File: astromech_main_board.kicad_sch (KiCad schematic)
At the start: 15 parts, among them IC2 MAX11645EUA+, J1 Screw_Terminal_01x02, J2 Screw_Terminal_01x02, J3 Screw_Terminal_01x02, U8 NCP1117-3.3_SOT223, U9 NCP1117-5.0_TO252

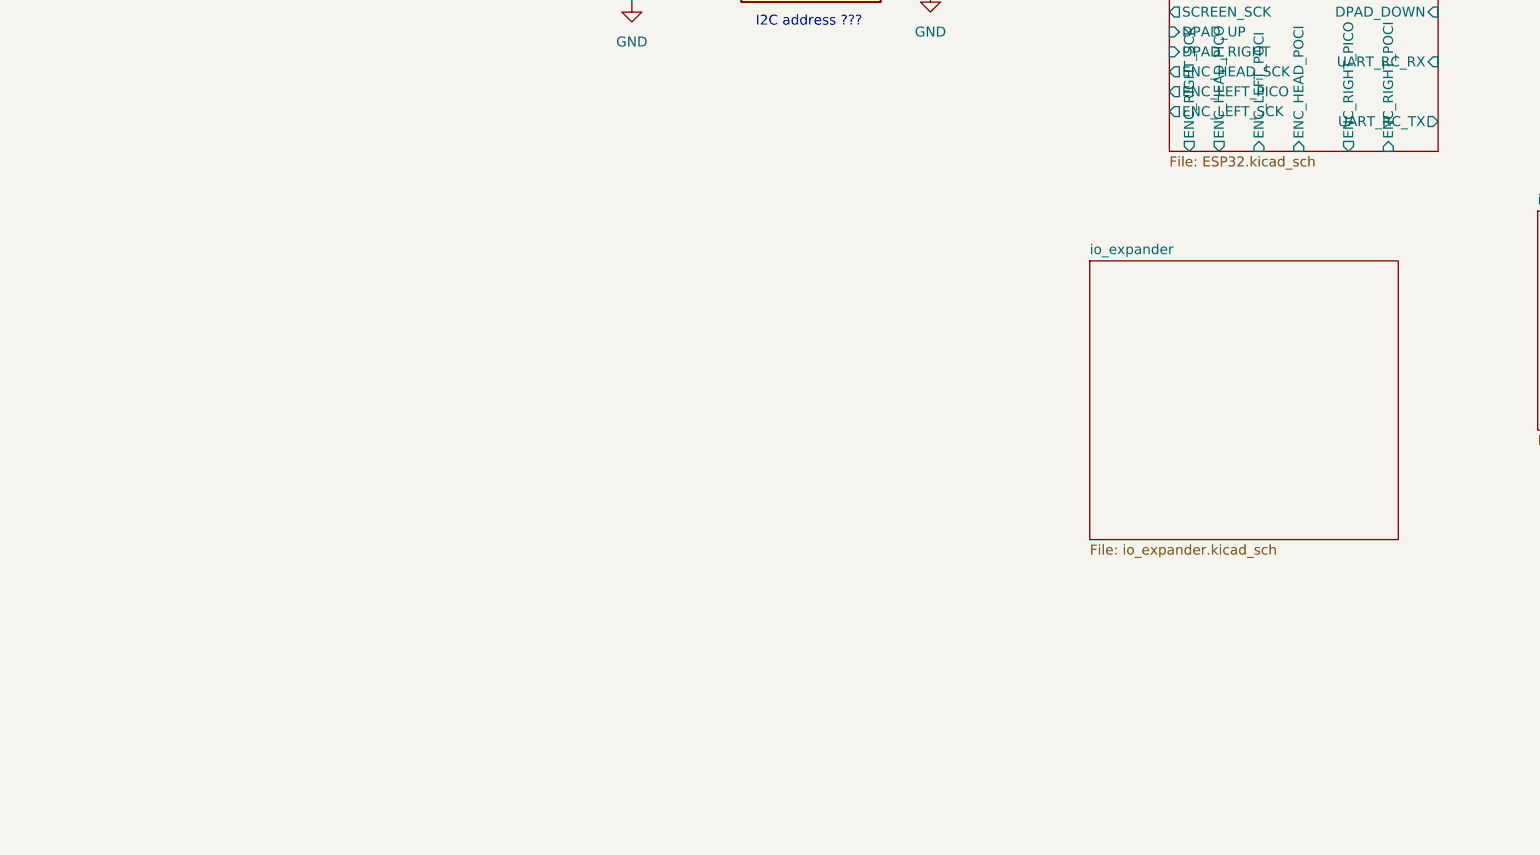
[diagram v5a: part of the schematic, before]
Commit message: moved io expander
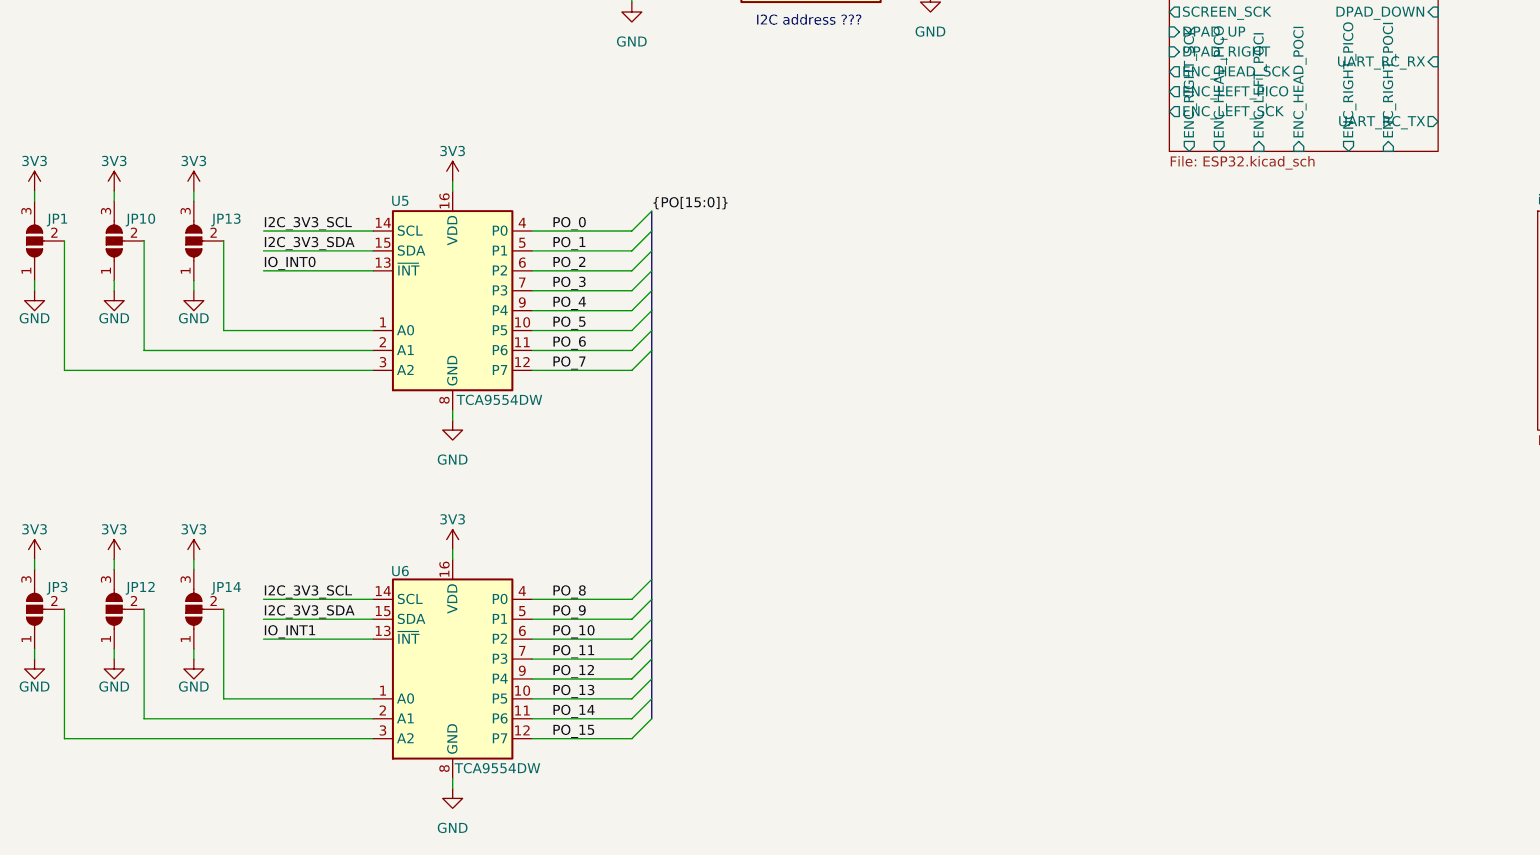
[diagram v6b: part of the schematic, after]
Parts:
- added JP1, JP10, JP12, JP13, JP14, JP3: SolderJumper_3_Open, symbol Jumper:SolderJumper_3_Open
- added U5, U6: TCA9554DW, Package_SO:SOIC-16W_7.5x10.3mm_P1.27mm, symbol Interface_Expansion:TCA9554DW
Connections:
- net 3V3: now also JP1.3 (B), JP10.3 (B), JP12.3 (B), JP13.3 (B), JP14.3 (B), JP3.3 (B), U5.16 (VDD), U6.16 (VDD)
- net GND: now also JP1.1 (A), JP10.1 (A), JP12.1 (A), JP13.1 (A), JP14.1 (A), JP3.1 (A), U5.8 (GND), U6.8 (GND)
- new net: JP1.2 (C), U5.3 (A2)
- new net: JP13.2 (C), U5.1 (A0)
- new net: JP14.2 (C), U6.1 (A0)
- new net: JP12.2 (C), U6.2 (A1)
- new net: JP3.2 (C), U6.3 (A2)
- new net: JP10.2 (C), U5.2 (A1)
- new net I2C_3V3_SCL: U5.14 (SCL), U6.14 (SCL)
- new net I2C_3V3_SDA: U5.15 (SDA), U6.15 (SDA)
- new net IO_INT0: U5.13 (~{INT})
- new net IO_INT1: U6.13 (~{INT})
- new net PO_0: U5.4 (P0)
- new net PO_1: U5.5 (P1)
- new net PO_10: U6.6 (P2)
- new net PO_11: U6.7 (P3)
- new net PO_12: U6.9 (P4)
- new net PO_13: U6.10 (P5)
- new net PO_14: U6.11 (P6)
- new net PO_15: U6.12 (P7)
- new net PO_2: U5.6 (P2)
- new net PO_3: U5.7 (P3)
- new net PO_4: U5.9 (P4)
- new net PO_5: U5.10 (P5)
- new net PO_6: U5.11 (P6)
- new net PO_7: U5.12 (P7)
- new net PO_8: U6.4 (P0)
- new net PO_9: U6.5 (P1)
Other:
- removed sheet io_expander

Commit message: moved encoder
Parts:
- added C2, C4: C_Small, symbol Device:C_Small
- added JP2, JP4, JP5, JP6: SolderJumper_2_Bridged, symbol Jumper:SolderJumper_2_Bridged
- added R6: R_Small_US, symbol Device:R_Small_US
- added R7: 1M, symbol Device:R_US
- added U10, U11, U7: LS7366R, LS7366R:DIP762W45P254L1917H533Q14, symbol LS7366R:LS7366R
- added U12: 74HC14, symbol 74xx:74HC14
- added Y1: Crystal, symbol Device:Crystal
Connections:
- net I2C_5V_SCL is gone; now on net I2C_3V3_SCL: IC2.5 (SCL)
- net I2C_5V_SDA is gone; now on net I2C_3V3_SDA: IC2.6 (SDA)
- net 3V3: now also IC2.8 (VDD), R6.1
- net 5V: now also U10.14 (VDD), U11.14 (VDD), U12.14 (VCC), U7.14 (VDD); no longer IC2.8 (VDD)
- net GND: now also C2.1, C4.1, U10.3 (VSS), U11.3 (VSS), U12.7 (GND), U7.3 (VSS)
- new net: JP5.1 (A), JP6.1 (A), U12.2
- new net: JP6.2 (B), U7.2 (FCKI)
- new net: C2.2, JP4.1 (A), R7.1, Y1.2
- new net: JP4.2 (B), U11.2 (FCKI)
- new net: C4.2, JP2.1 (A), R7.2, U12.1, Y1.1
- new net: JP5.2 (B), U10.2 (FCKI)
- new net: JP2.2 (B), U11.1 (FCKO)
- new net ENC_CNT_EN: U10.13 (CNT_EN), U11.13 (CNT_EN), U7.13 (CNT_EN)
- new net ENC_INT: R6.2, U10.8 (LFLAG/), U11.8 (LFLAG/), U7.8 (LFLAG/)
- new net HEAD_A: U11.12 (A)
- new net HEAD_B: U11.11 (B)
- new net HEAD_INDEX: U11.10 (INDEX/)
- new net LEFT_A: U10.12 (A)
- new net LEFT_B: U10.11 (B)
- new net LEFT_INDEX: U10.10 (INDEX/)
- new net RIGHT_A: U7.12 (A)
- new net RIGHT_B: U7.11 (B)
- new net RIGHT_INDEX: U7.10 (INDEX/)
- new net SPI_5V_CIPO: U10.6 (MISO), U11.6 (MISO), U7.6 (MISO)
- new net SPI_5V_COPI: U10.7 (MOSI), U11.7 (MOSI), U7.7 (MOSI)
- new net SPI_5V_CS_RIGHT: U10.4 (SS/), U11.4 (SS/), U7.4 (SS/)
- new net SPI_5V_SCK: U10.5 (SCK), U11.5 (SCK), U7.5 (SCK)
- no-connect marks 2 -> 15
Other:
- note added: "DONT FORGET PULL-UPS FOR I2C"
- note added: "HEAD ENCODER"
- note added: "LEFT ENCODER"
- note added: "RIGHT ENCODER"
- moved on the sheet: JP1, JP10, JP12, JP13, JP14, JP3, U5, U6

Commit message: Updated MCU
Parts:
- added U2: TCA9517ADGK, Package_SO:VSSOP-8_3x3mm_P0.65mm, symbol Logic_LevelTranslator:TCA9517ADGK
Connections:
- net 3V3: now also U2.1 (VCCA), U2.8 (VCCB)
- net GND: now also U2.4 (GND)
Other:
- removed sheet ESP32
- removed sheet hw_encoder
- removed sheet io_protection
- added sheet MCU (MCU.kicad_sch)
